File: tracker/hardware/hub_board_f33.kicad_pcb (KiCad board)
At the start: 2 copper layers, 75 x 55 mm, 14 parts, among them J1 SMA-868, J2 SMA-2G4, J3 SOLAR, U1 RP2040-Zero, U2 LoRa2021F33-2G4, U3 MAX-M10S, U4 MS5611, U5 TPS7A02

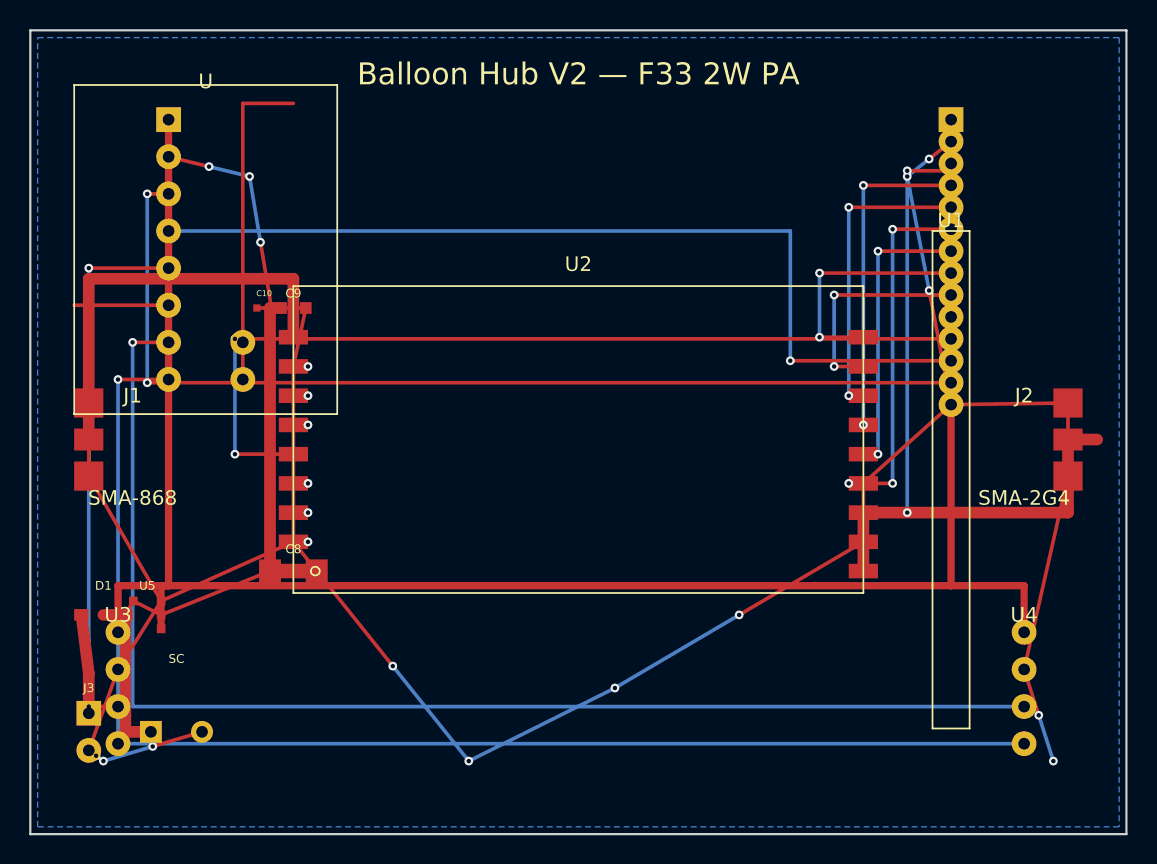
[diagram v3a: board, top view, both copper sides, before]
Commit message: fix(pcb): V1 clearance-aware routing — shorts 86→59, crossings 65→0
Router class routes all signals with collision detection:
- 3V3 power bus moved to B.Cu (eliminates power-signal conflicts)
- GND via stubs replace zone-dependent mesh
- Signal routing uses Router.connect() with detour/layer-switch fallback
- 85 segments, 64 vias, 22 warnings (10 forced)

Remaining: 43 unconnected (Router detour landing offsets), 59 shorts
(GND stubs through adjacent pads). Second-pass cleanup needed.

F33 board unchanged (uses original routing).
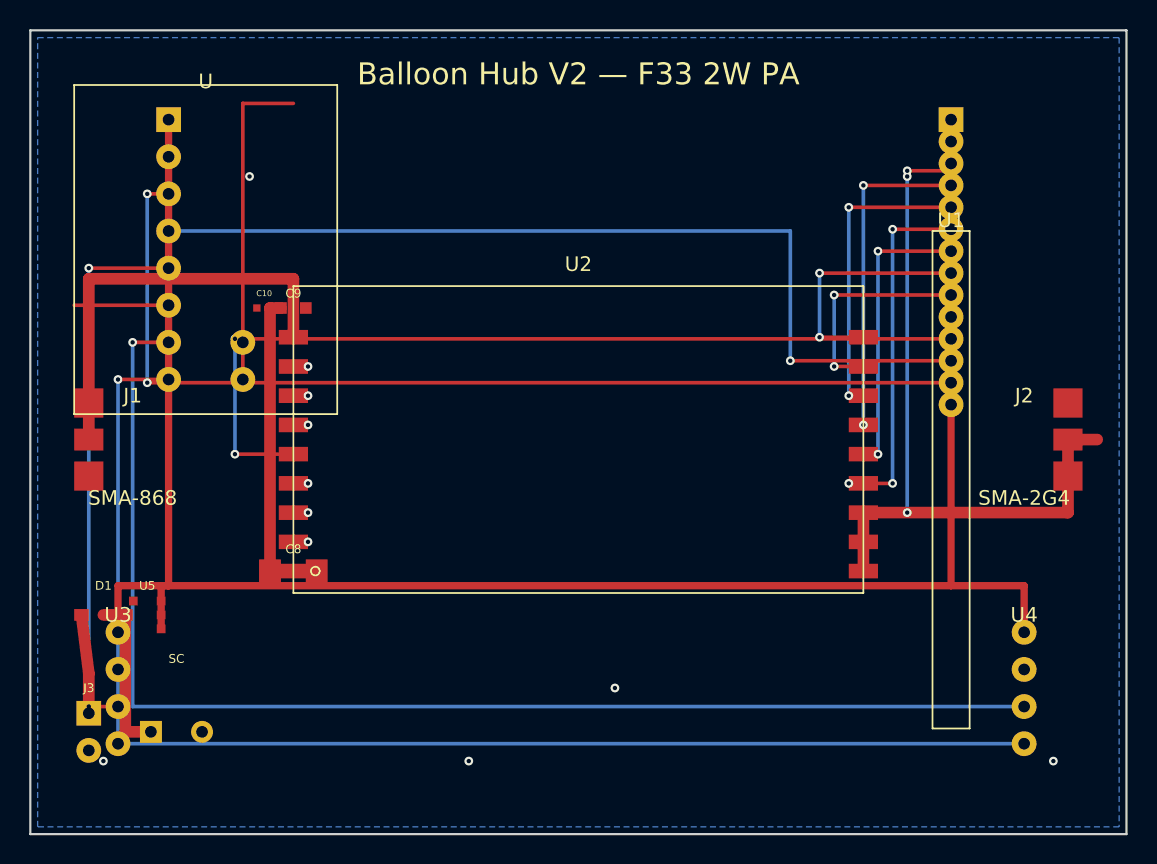
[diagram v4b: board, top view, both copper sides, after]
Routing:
- net GND: track 199.8 -> 7.00 mm, vias 22 -> 13
- net VCAP: track 43.8 -> 31.6 mm
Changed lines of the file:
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@@
     )
   )
-  (segment (start 4.0000 25.5000) (end 4.0000 30.5000) (width 0.25) (layer "F.Cu") (net 2))
-  (segment (start 4.0000 30.5000) (end 8.9500 39.0500) (width 0.25) (layer "F.Cu") (net 2))
-  (segment (start 4.0000 49.2700) (end 4.5000 49.6350) (width 0.25) (layer "F.Cu") (net 2))
-  (via (at 4.5000 49.6350) (size 0.6) (drill 0.3) (layers "F.Cu" "B.Cu") (net 2))
-  (segment (start 4.5000 49.6350) (end 5.0000 50.0000) (width 0.25) (layer "B.Cu") (net 2))
-  (segment (start 4.0000 49.2700) (end 6.0000 43.7300) (width 0.25) (layer "F.Cu") (net 2))
-  (segment (start 5.0000 50.0000) (end 8.3750 49.0000) (width 0.25) (layer "B.Cu") (net 2))
-  (via (at 8.3750 49.0000) (size 0.6) (drill 0.3) (layers "F.Cu" "B.Cu") (net 2))
-  (segment (start 8.3750 49.0000) (end 11.7500 48.0000) (width 0.25) (layer "F.Cu") (net 2))
-  (segment (start 6.0000 43.7300) (end 8.9500 39.0500) (width 0.25) (layer "F.Cu") (net 2))
-  (segment (start 8.9500 39.0500) (end 18.0000 35.0000) (width 0.25) (layer "F.Cu") (net 2))
-  (segment (start 9.4600 8.6500) (end 12.2300 9.3250) (width 0.25) (layer "F.Cu") (net 2))
-  (via (at 12.2300 9.3250) (size 0.6) (drill 0.3) (layers "F.Cu" "B.Cu") (net 2))
-  (segment (start 12.2300 9.3250) (end 15.0000 10.0000) (width 0.25) (layer "B.Cu") (net 2))
-  (segment (start 15.0000 10.0000) (end 15.7500 14.5000) (width 0.25) (layer "B.Cu") (net 2))
-  (via (at 15.7500 14.5000) (size 0.6) (drill 0.3) (layers "F.Cu" "B.Cu") (net 2))
-  (segment (start 15.7500 14.5000) (end 16.5000 19.0000) (width 0.25) (layer "F.Cu") (net 2))
-  (segment (start 18.0000 25.0000) (end 18.0000 23.0000) (width 0.25) (layer "F.Cu") (net 2))
-  (segment (start 18.0000 27.0000) (end 18.0000 25.0000) (width 0.25) (layer "F.Cu") (net 2))
-  (segment (start 18.0000 27.0000) (end 18.0000 31.0000) (width 0.25) (layer "F.Cu") (net 2))
-  (segment (start 18.0000 33.0000) (end 18.0000 35.0000) (width 0.25) (layer "F.Cu") (net 2))
-  (segment (start 18.8500 19.0000) (end 16.5000 19.0000) (width 0.25) (layer "F.Cu") (net 2))
-  (segment (start 18.8500 19.0000) (end 18.0000 23.0000) (width 0.25) (layer "F.Cu") (net 2))
-  (segment (start 18.0000 31.0000) (end 18.0000 33.0000) (width 0.25) (layer "F.Cu") (net 2))
-  (segment (start 19.6000 37.0000) (end 18.0000 35.0000) (width 0.25) (layer "F.Cu") (net 2))
-  (segment (start 19.6000 37.0000) (end 24.8000 43.5000) (width 0.25) (layer "F.Cu") (net 2))
-  (via (at 24.8000 43.5000) (size 0.6) (drill 0.3) (layers "F.Cu" "B.Cu") (net 2))
-  (segment (start 24.8000 43.5000) (end 30.0000 50.0000) (width 0.25) (layer "B.Cu") (net 2))
-  (segment (start 30.0000 50.0000) (end 40.0000 45.0000) (width 0.25) (layer "B.Cu") (net 2))
-  (segment (start 40.0000 45.0000) (end 48.5000 40.0000) (width 0.25) (layer "B.Cu") (net 2))
-  (via (at 48.5000 40.0000) (size 0.6) (drill 0.3) (layers "F.Cu" "B.Cu") (net 2))
-  (segment (start 48.5000 40.0000) (end 57.0000 35.0000) (width 0.25) (layer "F.Cu") (net 2))
-  (segment (start 57.0000 31.0000) (end 57.0000 35.0000) (width 0.25) (layer "F.Cu") (net 2))
-  (segment (start 60.0000 10.0000) (end 61.5000 17.8050) (width 0.25) (layer "B.Cu") (net 2))
-  (via (at 61.5000 17.8050) (size 0.6) (drill 0.3) (layers "F.Cu" "B.Cu") (net 2))
-  (segment (start 61.5000 17.8050) (end 63.0000 25.6100) (width 0.25) (layer "F.Cu") (net 2))
-  (segment (start 63.0000 7.6100) (end 61.5000 8.8050) (width 0.25) (layer "F.Cu") (net 2))
-  (via (at 61.5000 8.8050) (size 0.6) (drill 0.3) (layers "F.Cu" "B.Cu") (net 2))
-  (segment (start 61.5000 8.8050) (end 60.0000 10.0000) (width 0.25) (layer "B.Cu") (net 2))
-  (segment (start 63.0000 25.6100) (end 57.0000 31.0000) (width 0.25) (layer "F.Cu") (net 2))
-  (segment (start 70.0000 50.0000) (end 69.0000 46.8650) (width 0.25) (layer "B.Cu") (net 2))
-  (via (at 69.0000 46.8650) (size 0.6) (drill 0.3) (layers "F.Cu" "B.Cu") (net 2))
-  (segment (start 69.0000 46.8650) (end 68.0000 43.7300) (width 0.25) (layer "F.Cu") (net 2))
-  (segment (start 71.0000 25.5000) (end 63.0000 25.6100) (width 0.25) (layer "F.Cu") (net 2))
-  (segment (start 71.0000 30.5000) (end 71.0000 25.5000) (width 0.25) (layer "F.Cu") (net 2))
-  (segment (start 71.0000 30.5000) (end 68.0000 43.7300) (width 0.25) (layer "F.Cu") (net 2))
-  (segment (start 6.5000 40.0000) (end 7.0500 39.0500) (width 0.25) (layer "F.Cu") (net 21))
-  (segment (start 7.0500 39.0500) (end 8.9500 40.0000) (width 0.25) (layer "F.Cu") (net 21))
-  (segment (start 16.4000 19.0000) (end 15.5000 19.0000) (width 0.25) (layer "F.Cu") (net 21))
-  (segment (start 16.4000 37.0000) (end 8.9500 40.0000) (width 0.25) (layer "F.Cu") (net 21))
 )

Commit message: fix(pcb): F33 power bus to B.Cu + GND via relocation — shorts 27→19
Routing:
- net I2C_SCL: track 90.4 -> 63.6 mm, vias 2 -> 0
- net I2C_SDA: track 88.4 -> 63.6 mm, vias 2 -> 0
- net LR2021_CE: track 60.9 -> 45.1 mm, vias 2 -> 0
- net GND: track 7.00 -> 20.4 mm, vias 13 -> 15
- net SPI0_MISO: track 20.9 -> 10.6 mm, vias 2 -> 0
- net LR2021_BUSY: track 19.9 -> 9.72 mm, vias 2 -> 0
- net ESP_TX_RP2040_RX: track 69.4 -> 59.3 mm, vias 2 -> 0
- net SPI0_NSS: track 23.4 -> 13.6 mm, vias 2 -> 0
- net LR2021_IRQ: track 16.4 -> 6.66 mm, vias 2 -> 0
- net 3V3: track 135.6 -> 144.6 mm, vias 0 -> 5
- net LR2021_RST: track 14.9 -> 6.91 mm, vias 2 -> 0
- net SPI0_MOSI: track 22.4 -> 14.6 mm, vias 2 -> 0
- net GPS_TX_ESP_RX: track 37.5 -> 30.2 mm, vias 2 -> 0
- net SPI0_SCK: track 29.4 -> 22.6 mm, vias 2 -> 0
- net VCAP: track 31.6 -> 38.1 mm
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
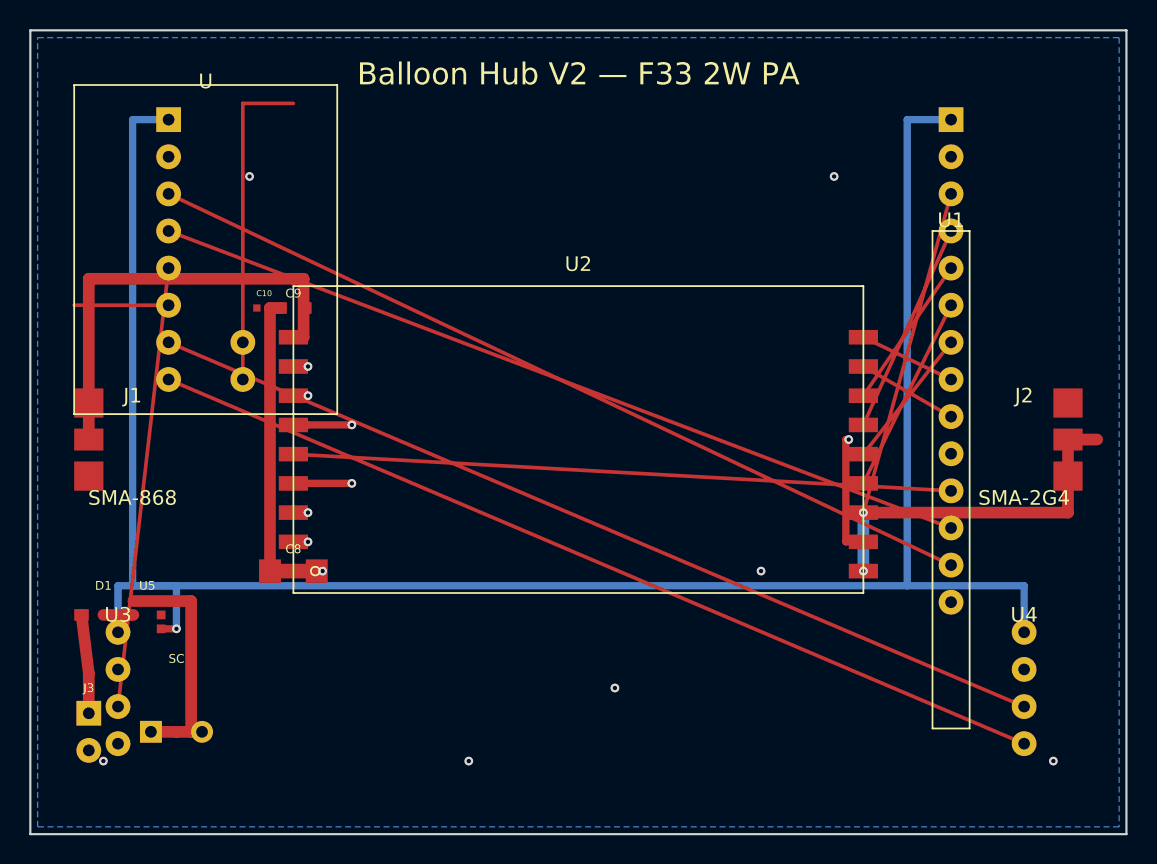
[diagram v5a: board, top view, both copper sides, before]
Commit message: fix(pcb): F33 B.Cu routing for power+UART+I2C — shorts 44→15, crossings 14→15
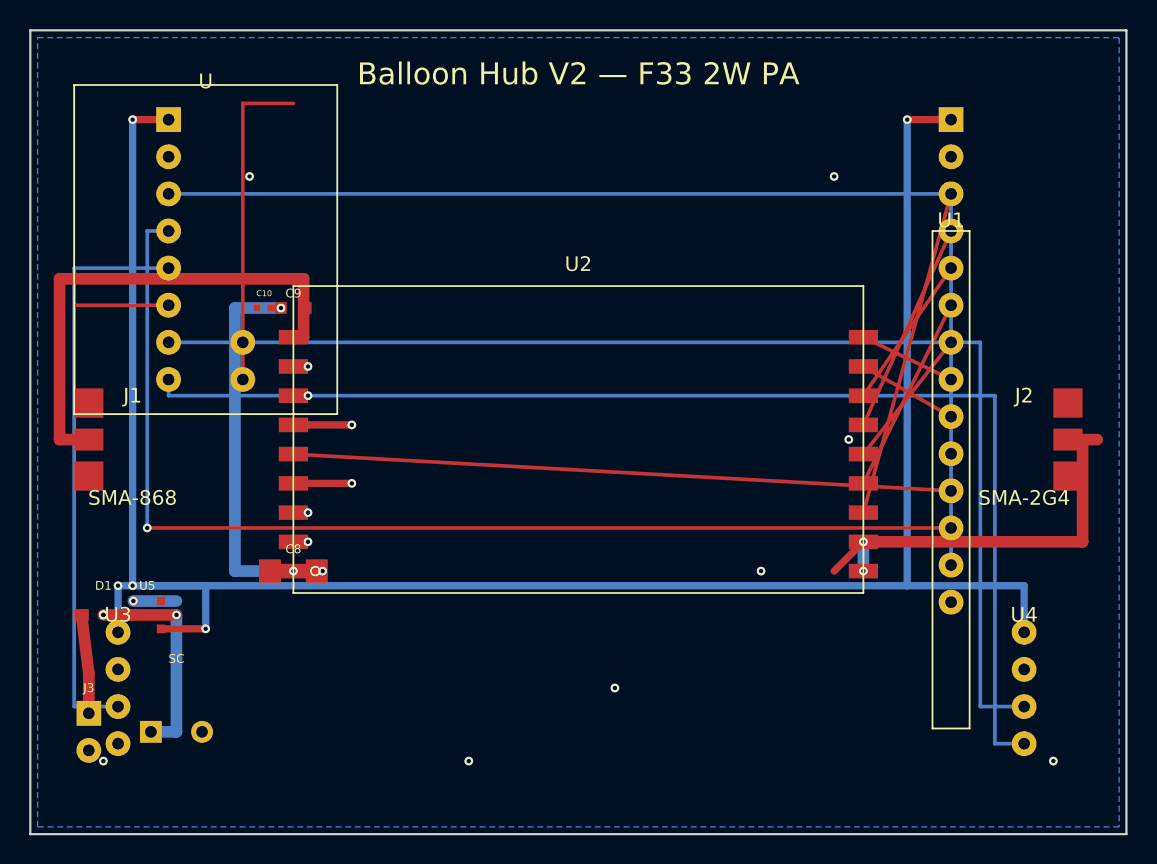
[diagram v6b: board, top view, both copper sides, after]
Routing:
- net I2C_SDA: track 63.6 -> 83.5 mm, vias 0 -> 2
- net I2C_SCL: track 63.6 -> 83.5 mm, vias 0 -> 2
- net ESP_TX_RP2040_RX: track 59.3 -> 78.9 mm, vias 0 -> 2
- net RP2040_TX_ESP_RX: track 57.3 -> 76.8 mm, vias 0 -> 4
- net GPS_TX_ESP_RX: track 30.2 -> 39.5 mm, vias 0 -> 2
- net GND: track 20.4 -> 14.8 mm
- net VCAP: track 38.1 -> 42.9 mm, vias 0 -> 7
- net RF_SUB_868: track 30.4 -> 34.4 mm
- net 3V3: track 144.6 -> 148.6 mm, vias 5 -> 10
